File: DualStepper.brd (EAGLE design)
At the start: 53.1 x 63 mm, 14 parts, among them X1 1751248, X2 1751248, X3 1751248, X4 1751248, X5 1751248

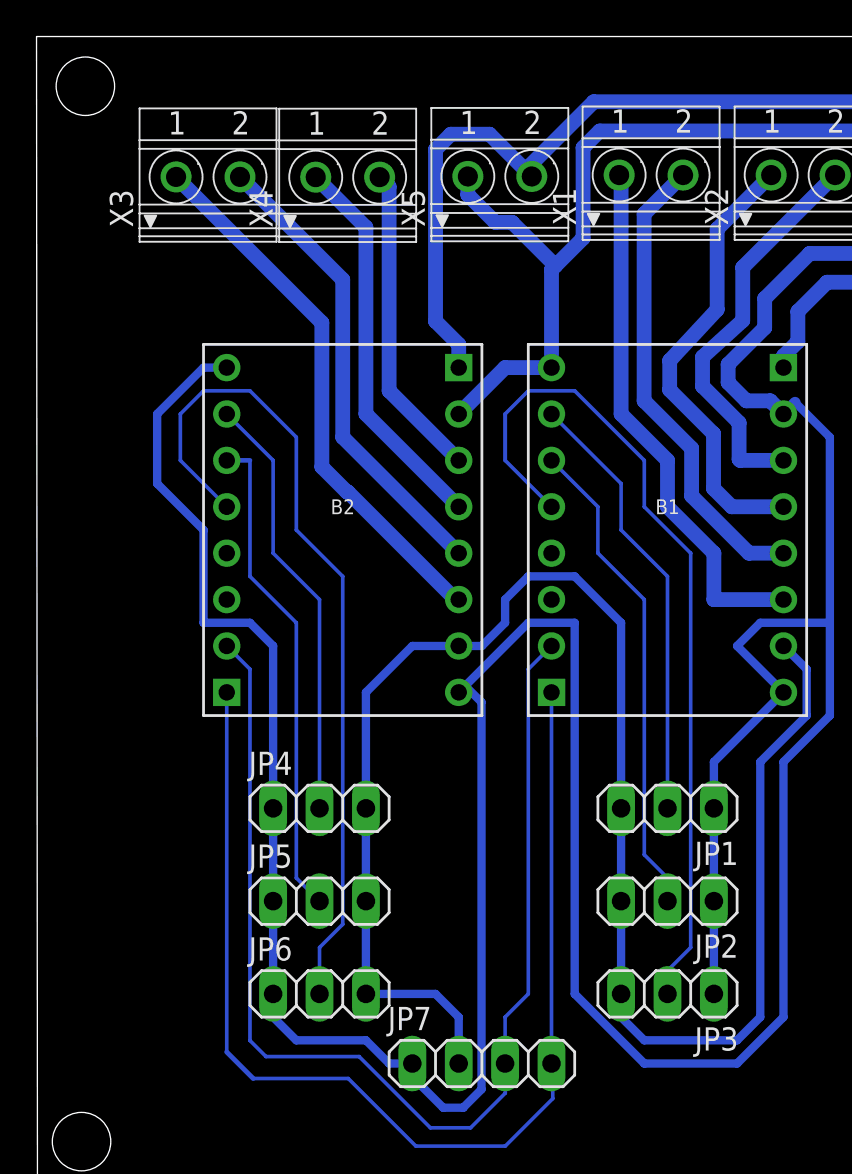
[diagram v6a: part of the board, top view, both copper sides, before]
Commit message: Added PartNaming
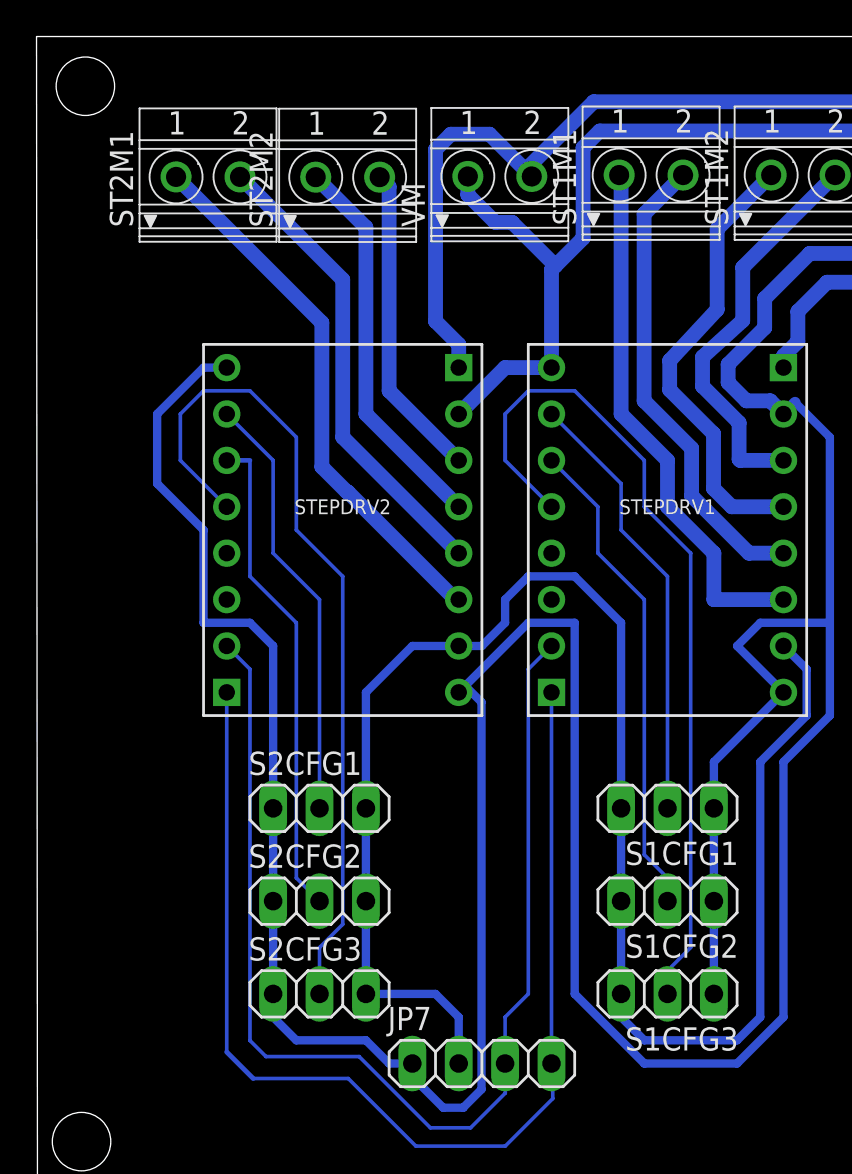
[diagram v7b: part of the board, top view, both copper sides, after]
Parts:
- renumbered B1 to STEPDRV1, B2 to STEPDRV2, JP1 to S1CFG1, JP2 to S1CFG2, JP3 to S1CFG3, JP4 to S2CFG1, JP5 to S2CFG2, JP6 to S2CFG3, X1 to ST1M1, X2 to ST1M2, X3 to ST2M1, X4 to ST2M2, X5 to VM

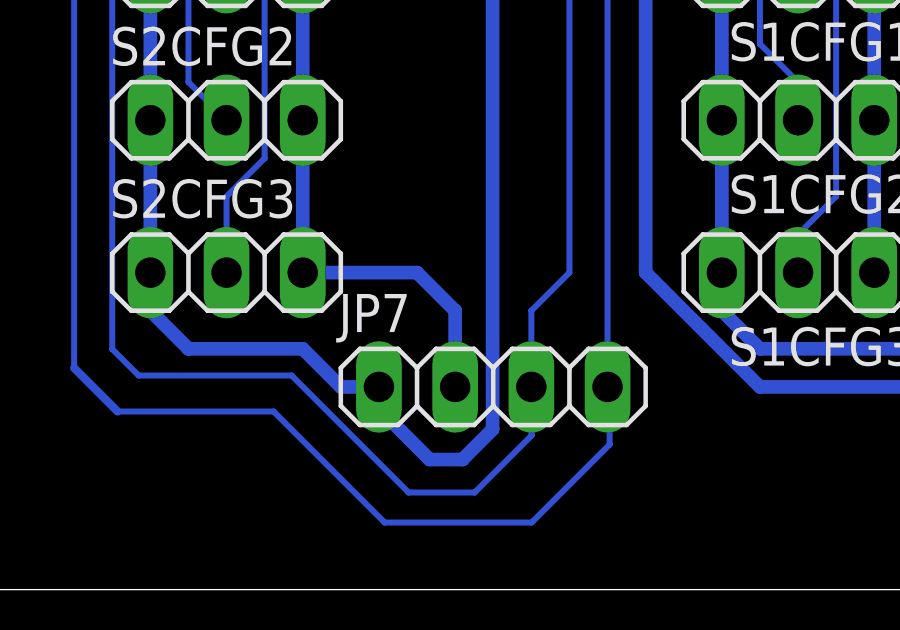
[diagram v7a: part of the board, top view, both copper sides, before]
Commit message: one Pin Namign added
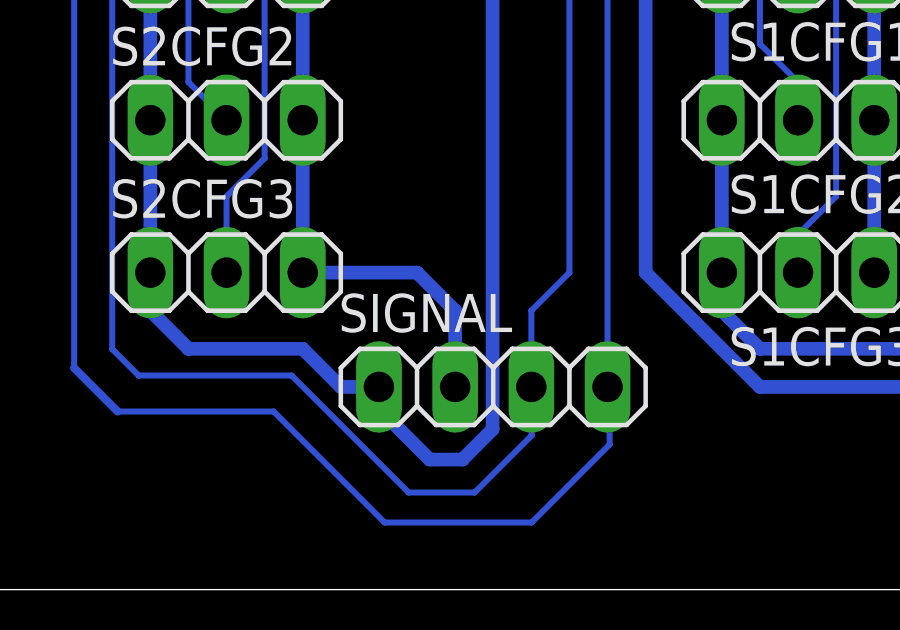
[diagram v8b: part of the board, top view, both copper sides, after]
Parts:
- renumbered JP7 to SIGNAL
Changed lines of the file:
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@@
 <attribute name="A1" value="" x="36.83" y="24.13" size="1.778" layer="27" display="off"/>
 </element>
-<element name="JP7" library="pinhead" package="1X04" value="" x="45.72" y="20.32"/>
+<element name="SIGNAL" library="pinhead" package="1X04" value="" x="45.72" y="20.32"/>
 <element name="ST1M1" library="con-phoenix-350" package="1751248" value="1751248" x="54.9832" y="69.0614">
 <attribute name="OC_NEWARK" value="unknown" x="54.9832" y="69.0614" size="1.778" layer="27" display="off"/>
@@
 <contactref element="S2CFG2" pad="1"/>
 <contactref element="S2CFG1" pad="1"/>
-<contactref element="JP7" pad="1"/>
+<contactref element="SIGNAL" pad="1"/>
 <contactref element="STEPDRV1" pad="EN"/>
 <contactref element="STEPDRV2" pad="EN"/>
@@
 <contactref element="S2CFG2" pad="3"/>
 <contactref element="S2CFG1" pad="3"/>
-<contactref element="JP7" pad="2"/>
+<contactref element="SIGNAL" pad="2"/>
 <wire x1="53.34" y1="24.13" x2="53.34" y2="22.86" width="0.4572" layer="16"/>
 <wire x1="53.34" y1="22.86" x2="54.61" y2="21.59" width="0.4572" layer="16"/>
@@
 <signal name="N$15">
 <contactref element="STEPDRV1" pad="DIR"/>
-<contactref element="JP7" pad="4"/>
+<contactref element="SIGNAL" pad="4"/>
 <contactref element="STEPDRV2" pad="DIR"/>
 <wire x1="49.53" y1="40.64" x2="49.53" y2="20.32" width="0.2" layer="16"/>
@@
 </signal>
 <signal name="N$16">
-<contactref element="JP7" pad="3"/>
+<contactref element="SIGNAL" pad="3"/>
 <contactref element="STEPDRV1" pad="STEP"/>
 <contactref element="STEPDRV2" pad="STEP"/>
